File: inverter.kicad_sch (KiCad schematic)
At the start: 2 parts

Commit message: added local lib as module
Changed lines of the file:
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@@
 		(on_board yes)
 		(dnp no)
+		(fields_autoplaced yes)
 		(property "Reference" "TB1"
-			(at 82.296 131.064 0)
-			(effects
-				(font
-					(size 1.27 1.27)
-				)
-				(justify left)
+			(at 85.09 133.3499 90)
+			(effects
+				(font
+					(size 1.27 1.27)
+				)
+				(justify right)
 			)
 		)
 		(property "Value" "STM32F4DISCOVERY"
-			(at 84.836 131.064 0)
-			(effects
-				(font
-					(size 1.27 1.27)
-				)
-				(justify left)
+			(at 85.09 135.8899 90)
+			(effects
+				(font
+					(size 1.27 1.27)
+				)
+				(justify right)
 			)
 		)
@@
 			)
 		)
+		(pin "P1_21"
+		)
+		(pin "P2_23"
+		)
+		(pin "P2_19"
+		)
+		(pin "P2_28"
+		)
+		(pin "P1_35"
+		)
+		(pin "P1_16"
+		)
+		(pin "P1_38"
+		)
+		(pin "P2_43"
+		)
+		(pin "P2_25"
+		)
+		(pin "P2_21"
+		)
+		(pin "P1_12"
+		)
+		(pin "P1_11"
+		)
+		(pin "P1_13"
+		)
 		(pin "P1_17"
 		)
-		(pin "P2_21"
+		(pin "P1_24"
+		)
+		(pin "P1_18"
+		)
+		(pin "P1_6"
+		)
+		(pin "P2_40"
 		)
 		(pin "P1_14"
 		)
-		(pin "P2_28"
-		)
-		(pin "P1_6"
-		)
-		(pin "P2_19"
-		)
-		(pin "P1_38"
-		)
-		(pin "P2_25"
+		(pin "P2_42"
+		)
+		(pin "P2_41"
+		)
+		(pin "P2_44"
+		)
+		(pin "P2_39"
+		)
+		(pin "P1_15"
+		)
+		(pin "P1_22"
 		)
 		(pin "P2_26"
 		)
-		(pin "P1_13"
-		)
-		(pin "P1_16"
-		)
-		(pin "P2_43"
-		)
-		(pin "P2_44"
-		)
-		(pin "P2_39"
-		)
-		(pin "P2_40"
-		)
-		(pin "P1_12"
-		)
-		(pin "P1_18"
-		)
-		(pin "P1_22"
-		)
-		(pin "P1_21"
-		)
-		(pin "P2_41"
-		)
-		(pin "P1_24"
-		)
-		(pin "P1_15"
-		)
-		(pin "P2_42"
-		)
-		(pin "P2_23"
-		)
-		(pin "P1_11"
-		)
 		(pin "P2_24"
 		)
@@
 		(pin "P1_34"
 		)
-		(pin "P1_35"
-		)
 		(pin "P1_36"
 		)
 		(pin "P1_37"
 		)
+		(pin "P1_10"
+		)
+		(pin "P1_4"
+		)
+		(pin "P1_3"
+		)
+		(pin "P2_46"
+		)
+		(pin "P2_9"
+		)
+		(pin "P2_32"
+		)
+		(pin "P2_30"
+		)
+		(pin "P1_39"
+		)
+		(pin "P2_12"
+		)
+		(pin "P2_3"
+		)
+		(pin "P1_7"
+		)
+		(pin "P2_45"
+		)
+		(pin "P2_38"
+		)
+		(pin "P2_4"
+		)
+		(pin "P1_8"
+		)
+		(pin "P2_5"
+		)
+		(pin "P1_19"
+		)
+		(pin "P2_36"
+		)
+		(pin "P2_47"
+		)
+		(pin "P2_37"
+		)
+		(pin "P1_20"
+		)
+		(pin "P1_9"
+		)
+		(pin "P2_10"
+		)
+		(pin "P2_48"
+		)
 		(pin "P2_35"
 		)
-		(pin "P2_38"
-		)
-		(pin "P1_7"
+		(pin "P2_6"
+		)
+		(pin "P2_22"
+		)
+		(pin "P2_33"
+		)
+		(pin "P2_34"
 		)
 		(pin "P2_31"
 		)
-		(pin "P2_10"
-		)
-		(pin "P2_46"
-		)
-		(pin "P1_10"
-		)
-		(pin "P1_39"
-		)
-		(pin "P2_48"
-		)
-		(pin "P2_47"
-		)
-		(pin "P2_12"
-		)
-		(pin "P2_3"
-		)
-		(pin "P1_4"
-		)
-		(pin "P2_37"
-		)
-		(pin "P2_5"
-		)
-		(pin "P2_6"
-		)
-		(pin "P1_8"
-		)
-		(pin "P1_9"
-		)
-		(pin "P1_20"
-		)
-		(pin "P2_45"
-		)
-		(pin "P2_4"
-		)
-		(pin "P2_22"
-		)
-		(pin "P2_36"
-		)
-		(pin "P1_3"
-		)
-		(pin "P1_19"
-		)
-		(pin "P2_9"
-		)
-		(pin "P2_33"
-		)
-		(pin "P2_34"
-		)
-		(pin "P2_32"
-		)
-		(pin "P2_30"
+		(pin "P2_29"
 		)
 		(pin "P2_27"
 		)
-		(pin "P2_29"
-		)
 		(pin "P1_40"
 		)
 		(pin "P1_32"
 		)
+		(pin "P1_28"
+		)
+		(pin "P1_27"
+		)
+		(pin "P1_47"
+		)
+		(pin "P1_30"
+		)
+		(pin "P1_5"
+		)
+		(pin "P1_49"
+		)
+		(pin "P2_18"
+		)
+		(pin "P1_33"
+		)
+		(pin "P1_42"
+		)
+		(pin "P1_43"
+		)
+		(pin "P1_46"
+		)
 		(pin "P2_15"
 		)
+		(pin "P2_13"
+		)
+		(pin "P1_45"
+		)
+		(pin "P1_25"
+		)
+		(pin "P1_44"
+		)
+		(pin "P2_11"
+		)
+		(pin "P1_26"
+		)
+		(pin "P2_14"
+		)
+		(pin "P2_17"
+		)
+		(pin "P1_41"
+		)
+		(pin "P1_31"
+		)
+		(pin "P2_16"
+		)
+		(pin "P1_29"
+		)
 		(pin "P2_7"
 		)
+		(pin "P2_8"
+		)
+		(pin "P1_1"
+		)
 		(pin "P1_2"
 		)
-		(pin "P1_44"
-		)
-		(pin "P2_14"
-		)
-		(pin "P1_27"
-		)
-		(pin "P1_30"
-		)
-		(pin "P2_18"
-		)
-		(pin "P1_46"
-		)
-		(pin "P1_42"
-		)
-		(pin "P1_26"
-		)
-		(pin "P2_17"
-		)
-		(pin "P2_16"
-		)
-		(pin "P1_28"
-		)
-		(pin "P2_13"
-		)
-		(pin "P1_41"
-		)
-		(pin "P1_45"
-		)
-		(pin "P2_11"
-		)
-		(pin "P1_47"
-		)
-		(pin "P1_25"
-		)
-		(pin "P1_31"
-		)
-		(pin "P1_33"
-		)
-		(pin "P1_29"
-		)
-		(pin "P1_43"
-		)
-		(pin "P2_8"
-		)
-		(pin "P1_1"
-		)
-		(pin "P1_5"
+		(pin "P1_23"
+		)
+		(pin "P1_50"
+		)
+		(pin "P2_2"
 		)
 		(pin "P2_49"
 		)
+		(pin "P2_50"
+		)
 		(pin "P2_1"
 		)
-		(pin "P2_2"
-		)
-		(pin "P1_50"
-		)
-		(pin "P1_23"
-		)
-		(pin "P1_49"
-		)
-		(pin "P2_50"
-		)
 		(instances

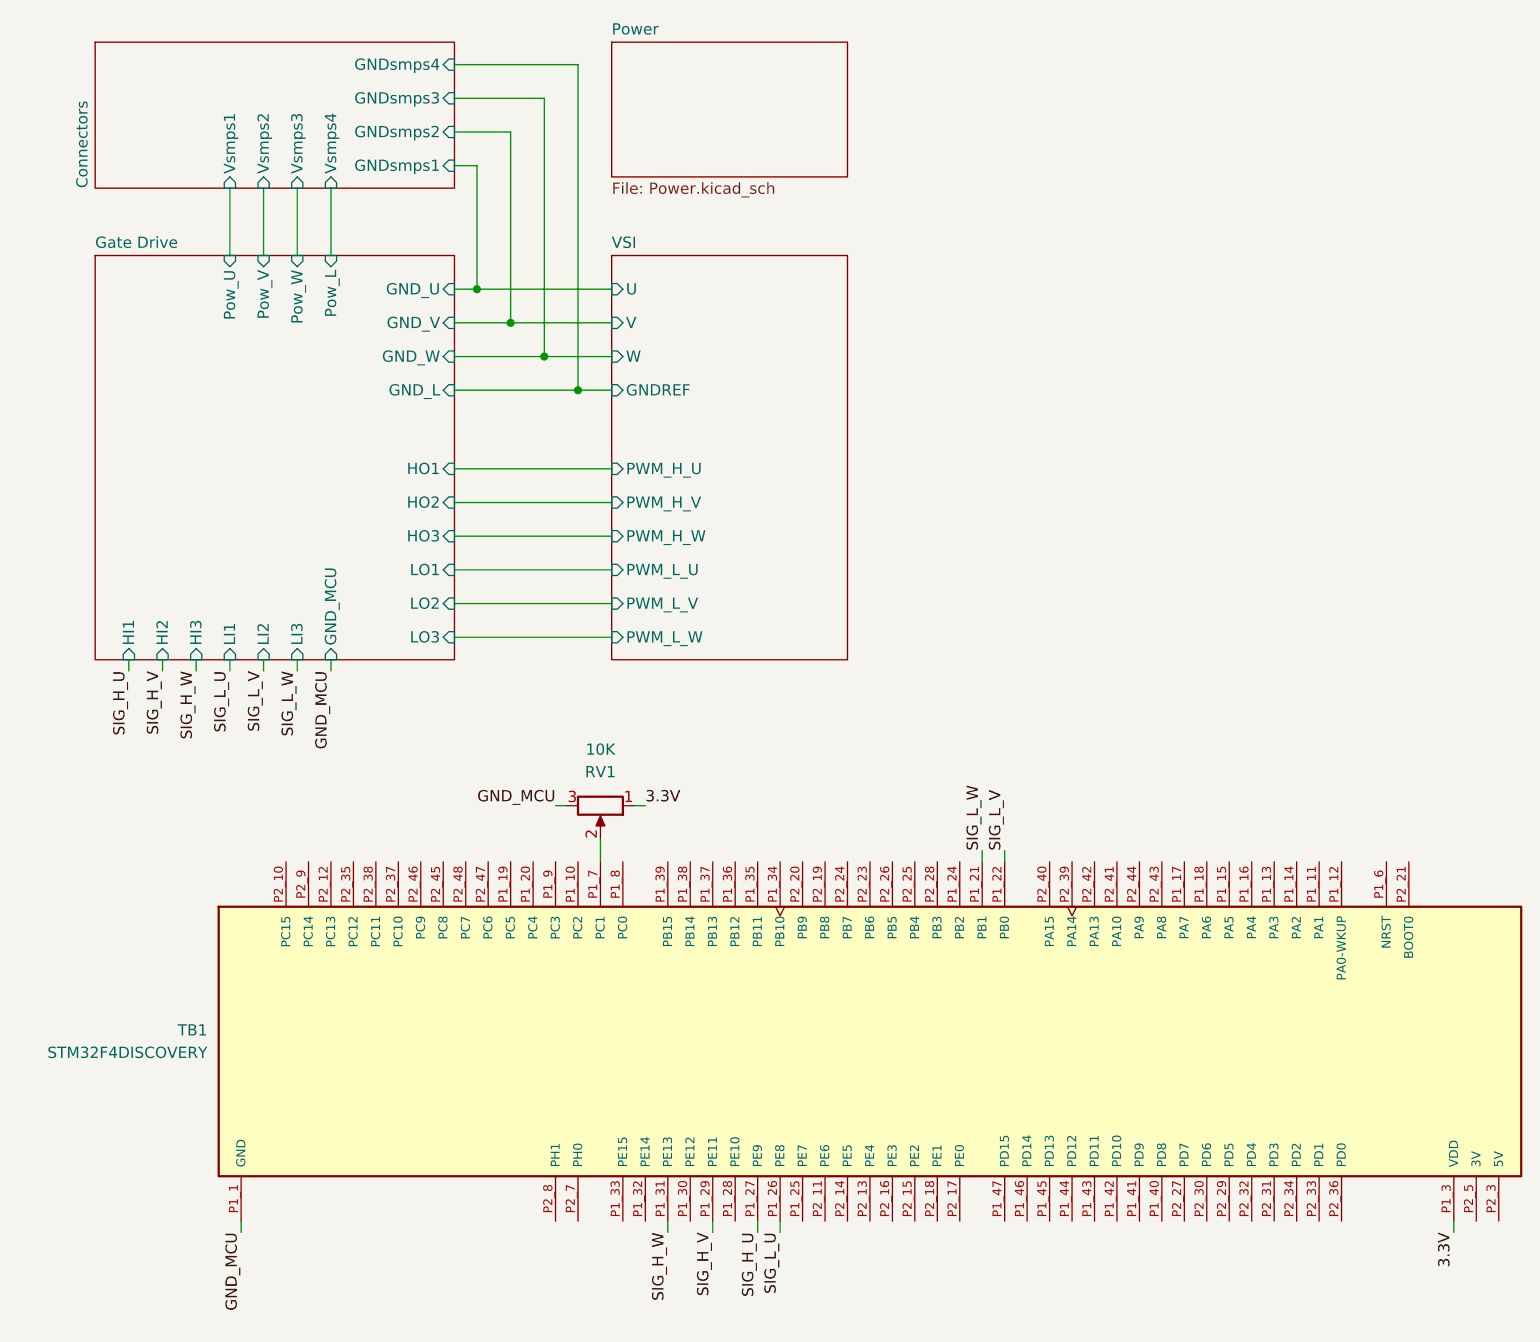
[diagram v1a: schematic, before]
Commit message: dev: added NC flags and fixed ERC warnings. Added custom design rules for PCB Design.
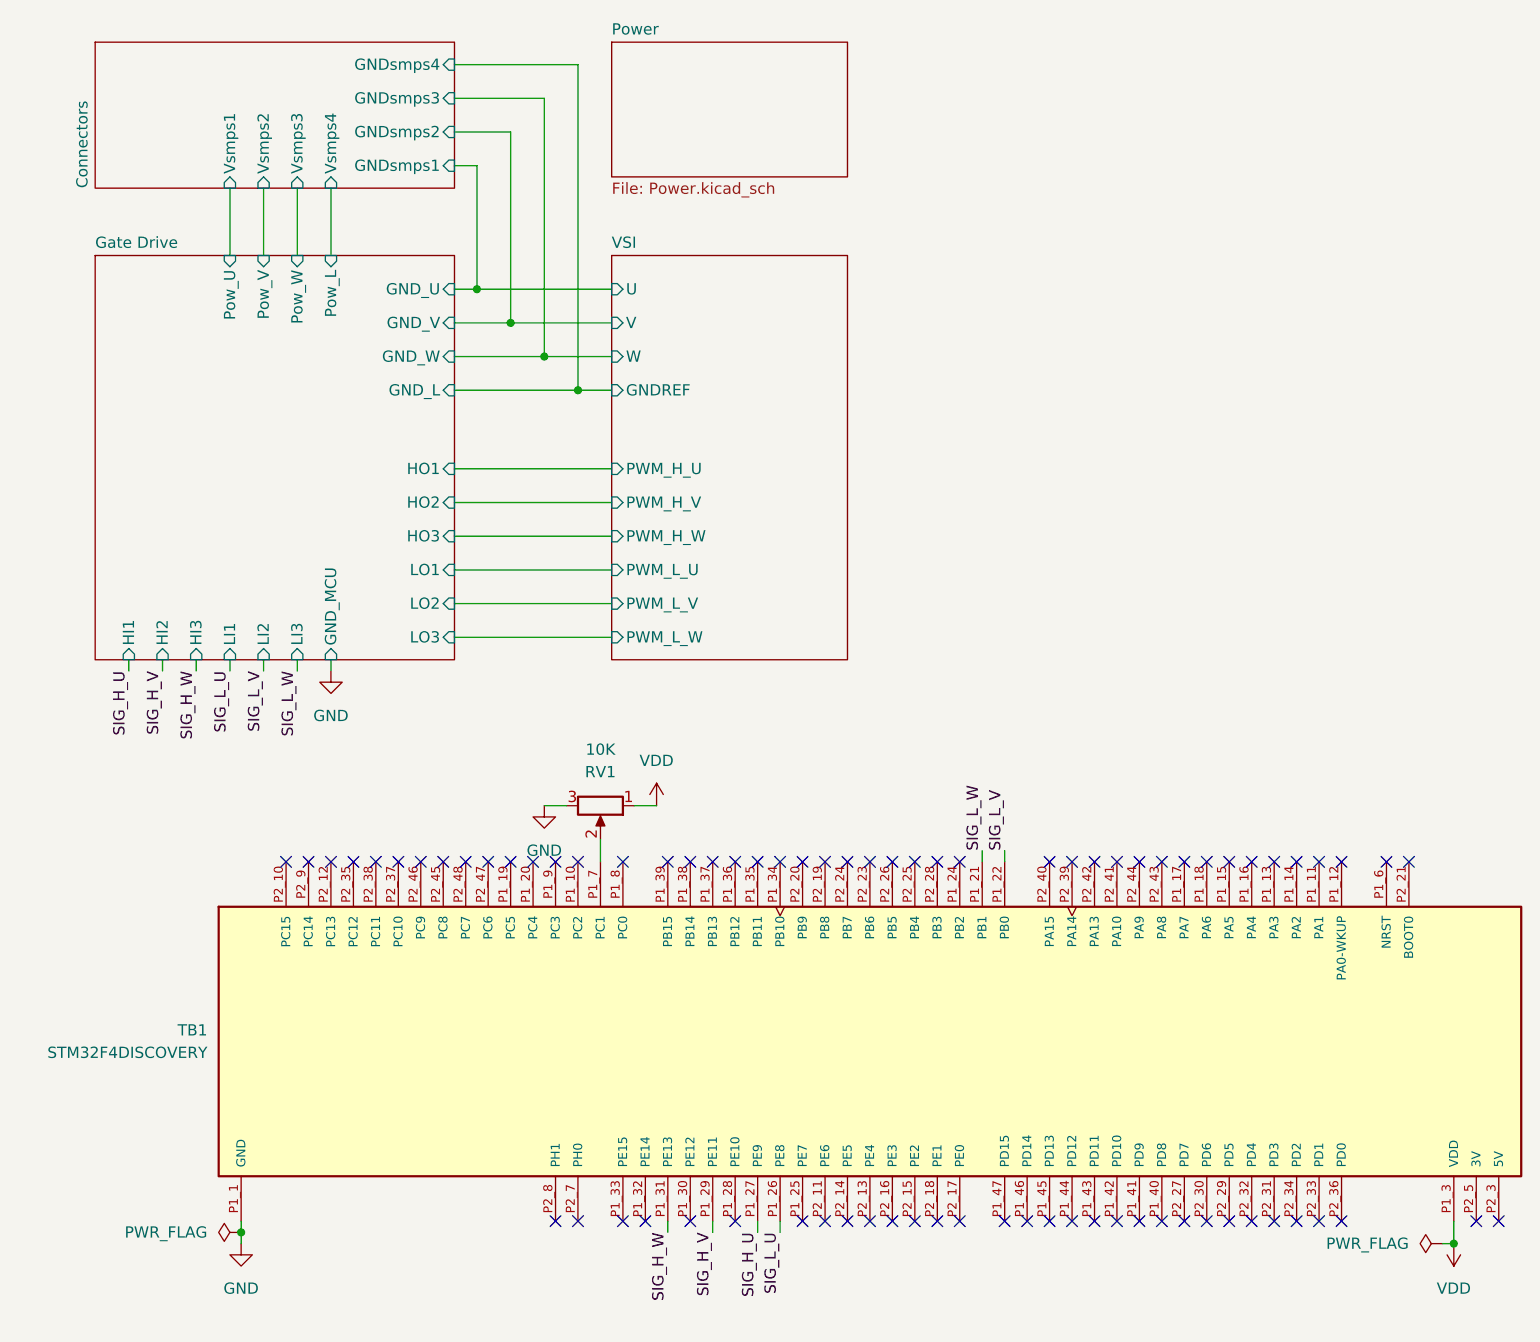
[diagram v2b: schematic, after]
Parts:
- RV1: footprint (none) -> Potentiometer_THT:Potentiometer_Alps_RK09K_Single_Horizontal
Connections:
- no-connect marks 0 -> 77
